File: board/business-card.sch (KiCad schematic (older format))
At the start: 36 parts, among them J1 Conn_01x06, SW1 SW_SPDT, SW2 Mutual_Capacitance_Button, SW3 Mutual_Capacitance_Button, SW4 Mutual_Capacitance_Button, SW5 Mutual_Capacitance_Button, SW6 Mutual_Capacitance_Button, SW7 Mutual_Capacitance_Button, U1 ATtiny1616-S

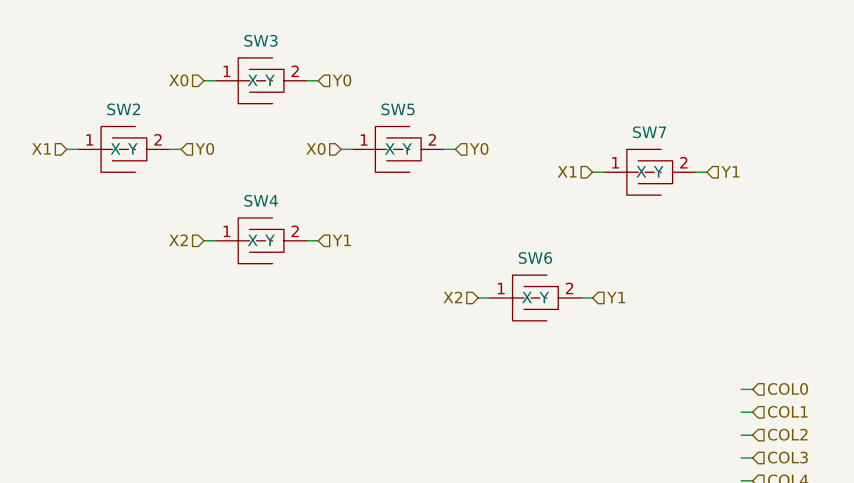
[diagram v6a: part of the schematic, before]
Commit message: Updated footprints for mcu and switch.
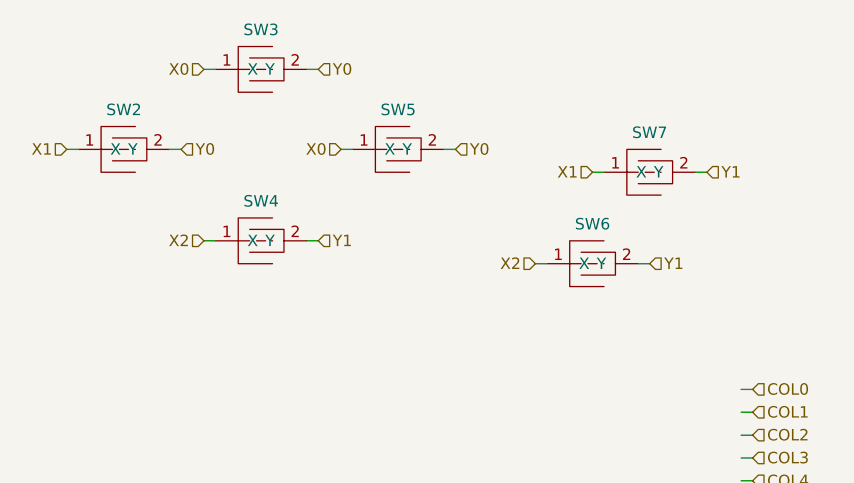
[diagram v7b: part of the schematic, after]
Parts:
- SW1: footprint colinholzman:JSX08001SAQNL-through-board-mount -> colinholzman:JSX08001SAQNL_through_board_mount
- U1: footprint Package_SO:SOIC-20W_7.5x12.8mm_P1.27mm -> colinholzman:SOIC-20W_7.5x12.8mm_P1.27mm_through_board_mount
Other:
- moved on the sheet: SW3, SW6
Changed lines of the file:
@@
 F 0 "U1" H 3800 5300 50  0000 C CNN
 F 1 "ATtiny1616-S" H 4650 5300 50  0000 C CNN
-F 2 "Package_SO:SOIC-20W_7.5x12.8mm_P1.27mm" H 4250 4450 50  0001 C CIN
+F 2 "colinholzman:SOIC-20W_7.5x12.8mm_P1.27mm_through_board_mount" H 4250 4450 50  0001 C CIN
 F 3 "http://ww1.microchip.com/downloads/en/DeviceDoc/ATtiny3216_ATtiny1616-data-sheet-40001997B.pdf" H 4250 4450 50  0001 C CNN
 	1    4250 4450
@@
 	5100 4850 5150 4850
 Wire Wire Line
-	2850 1000 2900 1000
+	2850 950  2900 950
 Wire Wire Line
 	2250 1300 2300 1300
@@
 	4550 1400 4600 1400
 Wire Wire Line
-	4050 1950 4100 1950
-Text HLabel 2850 1000 0    50   Input ~ 0
+	4300 1800 4350 1800
+Text HLabel 2850 950  0    50   Input ~ 0
 X0
 Text HLabel 2250 1300 0    50   Input ~ 0
@@
 Text HLabel 4550 1400 0    50   Input ~ 0
 X1
-Text HLabel 4050 1950 0    50   Input ~ 0
+Text HLabel 4300 1800 0    50   Input ~ 0
 X2
 Wire Wire Line
-	3350 1000 3300 1000
+	3350 950  3300 950
 Wire Wire Line
 	3950 1300 3900 1300
@@
 Wire Wire Line
 	5050 1400 5000 1400
-Text HLabel 3350 1000 2    50   Input ~ 0
+Text HLabel 3350 950  2    50   Input ~ 0
 Y0
 Text HLabel 3950 1300 2    50   Input ~ 0
@@
 Text HLabel 3350 1700 2    50   Input ~ 0
 Y1
-Text HLabel 4550 1950 2    50   Input ~ 0
+Text HLabel 4800 1800 2    50   Input ~ 0
 Y1
 Wire Wire Line
-	4500 1950 4550 1950
+	4750 1800 4800 1800
 $Comp
 L colinholzman:Mutual_Capacitance_Button SW2
@@
 L colinholzman:Mutual_Capacitance_Button SW3
 U 1 1 6094A060
-P 3100 1000
-F 0 "SW3" H 3100 1173 50  0000 C CNN
-F 1 "Mutual_Capacitance_Button" H 3100 1174 50  0001 C CNN
-F 2 "colinholzman:Mutual_Capacitance_Button" H 3100 1000 50  0001 C CNN
-F 3 "" H 3100 1000 50  0001 C CNN
-	1    3100 1000
+P 3100 950
+F 0 "SW3" H 3100 1123 50  0000 C CNN
+F 1 "Mutual_Capacitance_Button" H 3100 1124 50  0001 C CNN
+F 2 "colinholzman:Mutual_Capacitance_Button" H 3100 950 50  0001 C CNN
+F 3 "" H 3100 950 50  0001 C CNN
+	1    3100 950
 	1    0    0    -1
 $EndComp
@@
 L colinholzman:Mutual_Capacitance_Button SW6
 U 1 1 6095053F
-P 4300 1950
-F 0 "SW6" H 4300 2123 50  0000 C CNN
-F 1 "Mutual_Capacitance_Button" H 4300 2124 50  0001 C CNN
-F 2 "colinholzman:Mutual_Capacitance_Button" H 4300 1950 50  0001 C CNN
-F 3 "" H 4300 1950 50  0001 C CNN
-	1    4300 1950
+P 4550 1800
+F 0 "SW6" H 4550 1973 50  0000 C CNN
+F 1 "Mutual_Capacitance_Button" H 4550 1974 50  0001 C CNN
+F 2 "colinholzman:Mutual_Capacitance_Button" H 4550 1800 50  0001 C CNN
+F 3 "" H 4550 1800 50  0001 C CNN
+	1    4550 1800
 	1    0    0    -1
 $EndComp
@@
 F 0 "SW1" V 1246 1662 50  0000 R CNN
 F 1 "SW_SPDT" V 1155 1662 50  0000 R CNN
-F 2 "colinholzman:JSX08001SAQNL-through-board-mount" H 1200 1850 50  0001 C CNN
+F 2 "colinholzman:JSX08001SAQNL_through_board_mount" H 1200 1850 50  0001 C CNN
 F 3 "~" H 1200 1850 50  0001 C CNN
 F 4 "C&K" H 1200 1850 50  0001 C CNN "mfg1"

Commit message: Added business card specific footprints to business-card.pretty lib.
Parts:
- BT1: footprint renata:CR1216_MFR_SM -> business-card:CR2016_MFR_SM_through_board_mount
- SW1: footprint colinholzman:JSX08001SAQNL_through_board_mount -> business-card:JSX08001SAQNL_through_board_mount
- U1: footprint colinholzman:SOIC-20W_7.5x12.8mm_P1.27mm_through_board_mount -> business-card:SOIC-20W_7.5x12.8mm_P1.27mm_through_board_mount
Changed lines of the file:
@@
 F 0 "BT1" H 1318 2396 50  0000 L CNN
 F 1 "Battery_Cell" H 1318 2305 50  0000 L CNN
-F 2 "renata:CR1216_MFR_SM" V 1200 2360 50  0001 C CNN
+F 2 "business-card:CR2016_MFR_SM_through_board_mount" V 1200 2360 50  0001 C CNN
 F 3 "~" V 1200 2360 50  0001 C CNN
 	1    1200 2300
@@
 F 0 "U1" H 3800 5300 50  0000 C CNN
 F 1 "ATtiny1616-S" H 4650 5300 50  0000 C CNN
-F 2 "colinholzman:SOIC-20W_7.5x12.8mm_P1.27mm_through_board_mount" H 4250 4450 50  0001 C CIN
+F 2 "business-card:SOIC-20W_7.5x12.8mm_P1.27mm_through_board_mount" H 4250 4450 50  0001 C CIN
 F 3 "http://ww1.microchip.com/downloads/en/DeviceDoc/ATtiny3216_ATtiny1616-data-sheet-40001997B.pdf" H 4250 4450 50  0001 C CNN
 	1    4250 4450
@@
 F 0 "SW1" V 1246 1662 50  0000 R CNN
 F 1 "SW_SPDT" V 1155 1662 50  0000 R CNN
-F 2 "colinholzman:JSX08001SAQNL_through_board_mount" H 1200 1850 50  0001 C CNN
+F 2 "business-card:JSX08001SAQNL_through_board_mount" H 1200 1850 50  0001 C CNN
 F 3 "~" H 1200 1850 50  0001 C CNN
 F 4 "C&K" H 1200 1850 50  0001 C CNN "mfg1"
